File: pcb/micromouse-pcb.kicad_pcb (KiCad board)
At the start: 4 copper layers, 100 x 114 mm, 154 parts, among them J1 JST_PH_B2B-PH-K_1x02_P2.00mm_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, J10 PinSocket_1x08_P2.54mm_Vertic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, J11 PinSocket_1x08_P2.54mm_Vertic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, J2 PinHeader_1x02_P2.54mm_Vertic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, J5 JST_PH_B6B-PH-K_1x06_P2.00mm_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, J6 JST_PH_B6B-PH-K_1x06_P2.00mm_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, J7 USB_C_Receptacle_GCT_USB4105-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, J8 PinHeader_1x06_P2.54mm_Vertic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, Q1 SOT-23, Q10 LED_1206_3216Metric, Q11 LED_1206_3216Metric, Q12 LED_1206_3216Metric, Q13 LED_1206_3216Metric, Q14 LED_1206_3216Metric, Q15 LED_1206_3216Metric, Q16 SOT-23, Q17 SOT-23, Q18 SOT-23, Q19 SOT-23, Q2 LED_D3.0mm_Clear, Q20 SOT-23, Q21 SOT-23, Q22 SOT-23, Q23 SOT-23, Q24 SOT-23, Q25 SOT-23, Q26 SOT-23, Q27 SOT-23, Q28 SOT-23, Q29 SOT-23, Q3 LED_D3.0mm_Clear, Q30 SOT-23, Q31 SOT-23, Q32 SOT-23, Q33 SOT-23, Q4 LED_D3.0mm_Clear, Q5 LED_D3.0mm_Clear, Q6 LED_D3.0mm_Clear, Q7 LED_D3.0mm_Clear, Q8 LED_1206_3216Metric, Q9 LED_1206_3216Metric, SW1 SW_PUSH_6mm, SW2 SW_PUSH_6mm, SW3 SW_PUSH_6mm, SW4 SW_PUSH_6mm, U1 Texas_DRC0010J_ThermalVias, U3 ESP32-S3-WROOM-1, U4 SOIC-24W_7.5x15.4mm_P1.27mm, U6 SOT-23-6

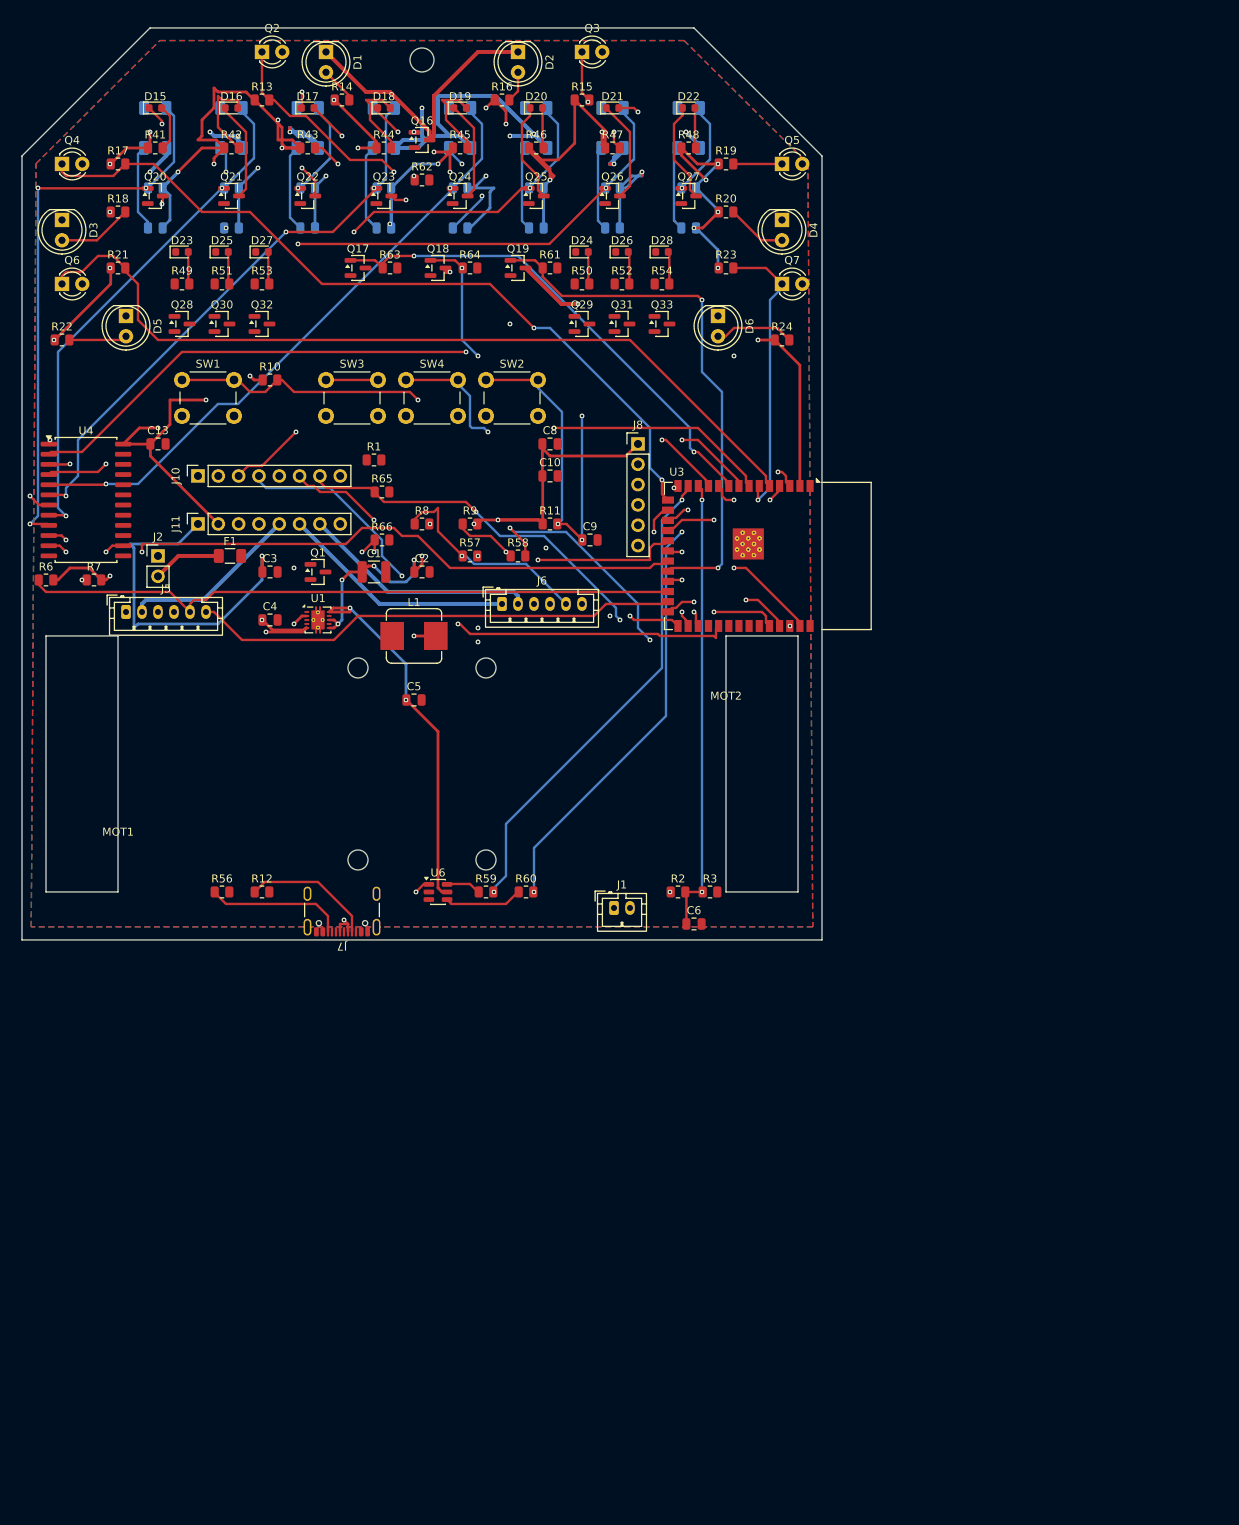
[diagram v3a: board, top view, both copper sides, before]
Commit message: Rev 5: SMD driver, rear service panel, bracket holes, routed to zero
- TB6612FNG as bare SSOP-24 in the inter-motor corridor; decoupling on B.Cu
- ESP32-S3-WROOM-1 moved to the rear, antenna overhanging the rear edge
  (Espressif-preferred); USB-C, ESD, JTAG and buttons A/B/C (+RST, silk
  letters) grouped around it as a service panel; motors moved forward
- Ø3.2mm/18.0mm-c-c NPTH pairs matching the printable UKMARSBot
  Pololu-pattern N20 bracket (STL link in README/PROJECT_NOTES)
- Wall sensors re-laid per parsed championship practice: detector forward,
  emitter 7.6mm behind, in-line, co-aimed; 10/45/75 degree aims
- USB VBUS turned into a cable-detect divider on IO37 (was a dangling NC)
- Board 100x120mm: +6mm rear fan-out band after routing proved density-bound
- board_geom.py: single source of mechanical truth (placement + router)
- Route-to-zero: jailed-first ordering with immediate retry ladders,
  hand bridges (D+ pair, VBUS stack link on In1), under-body pre-stitch,
  wide verify-proof retry rung, THT-aware clearance floors everywhere,
  all-layer via-replacement stitching, and heal_all.py convergent DRC healer
- Final: 0 unrouted, ERC 0, DRC 0 violations / 0 unconnected / 0 parity

Co-Authored-By: Claude Fable 5 <noreply@anthropic.com>
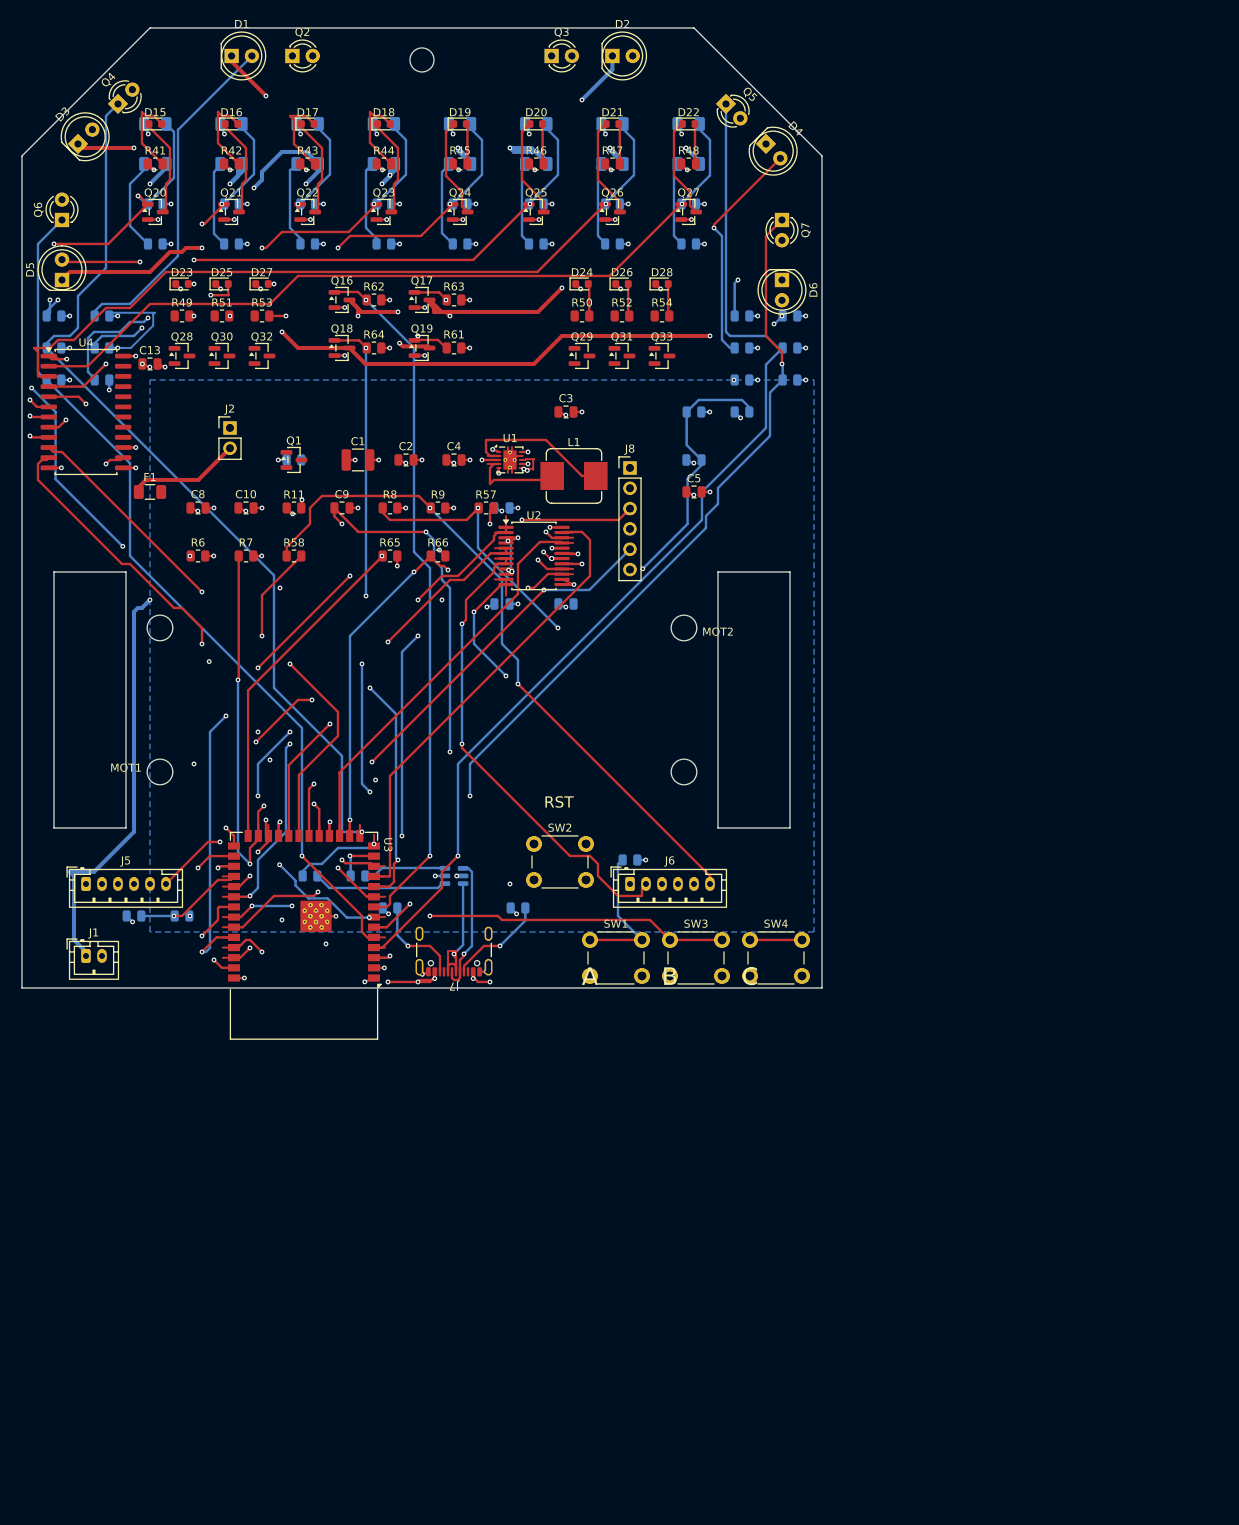
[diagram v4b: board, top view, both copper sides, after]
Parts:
- removed J10, J11: PinSocket_1x08_P2.54mm_Vertical, PinSocket_1x08_P2.54mm_Vertical
- added C11: 10uF, C_0805_2012Metric, B.Cu at (60.0, 72.0)
- added C12: 100nF, C_0805_2012Metric, B.Cu at (68.0, 72.0)
- added C14: 100nF, C_0805_2012Metric, B.Cu at (60.0, 60.0)
- added R67: R_0805_2012Metric, R_0805_2012Metric, B.Cu at (20.0, 111.0)
- added R68: R_0805_2012Metric, R_0805_2012Metric, B.Cu at (14.0, 111.0)
- added U2: SSOP-24_5.3x8.2mm_P0.65mm, SSOP-24_5.3x8.2mm_P0.65mm, F.Cu at (64.0, 66.0)
- C6, R1, R10, R12, R13, R14, R15, R16, R17, R18, R19, R2, R20, R21, R22, R23, R24, R3, R56, R59, R60, U6: moved to B.Cu
- moved SW1 86.6 mm to (71.0, 114.0)
- moved SW3 82.2 mm to (81.0, 114.0)
- moved SW4 82.2 mm to (91.0, 114.0)
- moved R10 75.0 mm to (76.0, 104.0), turned to 180 degrees
- moved U3 75.0 mm to (35.2, 113.5), turned to 180 degrees
- moved J1 66.3 mm to (8.00, 116.0)
- moved R3 60.1 mm to (90.0, 48.0), turned to 180 degrees
- moved R2 60.0 mm to (84.0, 48.0), turned to 180 degrees
- moved SW2 58.3 mm to (64.0, 102.0)
- moved C6 58.0 mm to (84.0, 54.0), turned to 180 degrees
- moved C8 44.7 mm to (22.0, 60.0)
- moved C5 43.6 mm to (84.0, 58.0)
- moved C3 42.1 mm to (68.0, 48.0)
- moved R14 40.4 mm to (10.0, 36.0), turned to 180 degrees
- moved R16 40.4 mm to (90.0, 36.0), turned to 180 degrees
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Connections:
- J7 pad A4: unconnected-(J7-VBUS-PadA4) -> USB_VBUS
- J7 pad A9: unconnected-(J7-VBUS-PadA4) -> USB_VBUS
- J7 pad B4: unconnected-(J7-VBUS-PadA4) -> USB_VBUS
- J7 pad B9: unconnected-(J7-VBUS-PadA4) -> USB_VBUS
- U3 pad 30: unconnected-(U3-IO37-Pad30) -> VBUS_SENSE
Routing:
- net PLUS3V3: track 602.5 -> 70.9 mm, vias 39 -> 54
- net VM_BATT: track 154.8 -> 19.6 mm, vias 9 -> 11
- net EMIT_DIAG_K: track 0.00 -> 111.3 mm, vias 0 -> 3
- net GND: track 0.00 -> 100.7 mm, vias 0 -> 69
- net JTAG_TDO: track 0.00 -> 93.1 mm, vias 0 -> 2
- net WALL4_SENSE: track 51.0 -> 134.5 mm
- net JTAG_TMS: track 0.00 -> 82.4 mm, vias 0 -> 1
- net JTAG_TCK: track 0.00 -> 79.2 mm, vias 0 -> 4
- net WALL2_SENSE: track 82.7 -> 161.6 mm, vias 2 -> 3
- net WALL6_SENSE: track 37.0 -> 113.6 mm, vias 1 -> 3
- net JTAG_TDI: track 0.00 -> 74.6 mm, vias 0 -> 4
- net ENC2_B: track 22.9 -> 85.1 mm, vias 1 -> 2
- net USB_VBUS: track 0.00 -> 56.6 mm, vias 0 -> 6
- net USB_DM: track 60.9 -> 5.54 mm, vias 2 -> 1
- net EMIT_FRONT_K: track 36.6 -> 91.3 mm, vias 0 -> 4
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- added copper zone on In1.Cu, net GND
- added copper zone on In2.Cu, net PLUS3V3
- added copper zone on B.Cu, net VM_BATT
- removed copper zone on B.Cu, net GND
- removed copper zone on F.Cu, net GND
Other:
- board size 100 x 114 mm -> 100 x 120 mm
- board text added: "A"
- board text added: "B"
- board text added: "C"
- board text added: "RST"

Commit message: Rev 5.1: fix floating FETs (audit-caught), NPTH bracket holes, hard gates
An adversarial audit of shipped rev 5 found Q1 + Q28-Q33 electrically
floating: Device:Q_PMOS numbers its pins D/G/S, the SOT-23 pads are 1/2/3,
and PcbGen silently skipped unmatched pads -- netless pads make no ratsnest,
so both the router and DRC connectivity were structurally blind. The battery
power path (J2 -> F1 -> Q1 -> VM_BATT) was open and all six wall-indicator
drivers were dead. Full postmortem in PROJECT_NOTES.md.

- QPMOS now instantiates Transistor_FET:Q_PMOS_GSD (pins 1/2/3, same
  geometry); netlist verified pin-by-pin, board rerouted to zero
- NEW hard gate: PcbGen.assert_netlist_pads_mapped() in build_pcb.py --
  every netlist (ref,pin) must exist as a board pad carrying that net
- net_conflict parity severity raised warning -> error in .kicad_pro
- verify_netlist.py rewritten for rev-5 topology (was rev-1 names, always
  exit 0); now checks the battery path and sensor->reader->indicator
  reachability, exits 1 on failure
- Mounting holes converted from Edge.Cuts circles to real NPTH pads
  (H1-H5, board-only footprints): drilled, in the fab hole table, matching
  the documented "Ø3.2mm NPTH" claim; keepouts now admit footprint pads
- heal_all.py: no more stacked bridge vias on unfixable fragments
- Docs: U3 anchor corrected to (35.25,113.5); stale rev-3/4 renders removed
- Verified: ERC 0 | DRC 0 violations / 0 unconnected / 0 parity (with
  net_conflict at error severity) | verify_netlist PASSES | 454/454 pins
  mapped | Q1 pads on Net-(Q1-G)/VM_BATT/Net-(Q1-D) with routed copper

Co-Authored-By: Claude Fable 5 <noreply@anthropic.com>
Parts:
- added H1: , MountingHole_NPTH, F.Cu at (17.2, 75.0)
- added H2: , MountingHole_NPTH, F.Cu at (17.2, 93.0)
- added H3: , MountingHole_NPTH, F.Cu at (82.8, 75.0)
- added H4: , MountingHole_NPTH, F.Cu at (82.8, 93.0)
- added H5: , MountingHole_NPTH, F.Cu at (50.0, 4.00)
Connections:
- F1 pad 2: Net-(F1-Pad2) -> Net-(Q1-D)
- Q1 pad 1: (no net) -> Net-(Q1-G)
- Q1 pad 2: (no net) -> VM_BATT
- Q1 pad 3: (no net) -> Net-(Q1-D)
- Q28 pad 1: (no net) -> WALL1_SENSE
- Q28 pad 2: (no net) -> PLUS3V3
- Q28 pad 3: (no net) -> Net-(Q28-D)
- Q29 pad 1: (no net) -> WALL2_SENSE
- Q29 pad 2: (no net) -> PLUS3V3
- Q29 pad 3: (no net) -> Net-(Q29-D)
- Q30 pad 1: (no net) -> WALL3_SENSE
- Q30 pad 2: (no net) -> PLUS3V3
- Q30 pad 3: (no net) -> Net-(Q30-D)
- Q31 pad 1: (no net) -> WALL4_SENSE
- Q31 pad 2: (no net) -> PLUS3V3
- Q31 pad 3: (no net) -> Net-(Q31-D)
- Q32 pad 1: (no net) -> WALL5_SENSE
- Q32 pad 2: (no net) -> PLUS3V3
- Q32 pad 3: (no net) -> Net-(Q32-D)
- Q33 pad 1: (no net) -> WALL6_SENSE
- Q33 pad 2: (no net) -> PLUS3V3
- Q33 pad 3: (no net) -> Net-(Q33-D)
- R1 pad 1: Net-(Q1-PadG) -> Net-(Q1-G)
- R49 pad 1: Net-(Q28-PadD) -> Net-(Q28-D)
- R50 pad 1: Net-(Q29-PadD) -> Net-(Q29-D)
- R51 pad 1: Net-(Q30-PadD) -> Net-(Q30-D)
- R52 pad 1: Net-(Q31-PadD) -> Net-(Q31-D)
- R53 pad 1: Net-(Q32-PadD) -> Net-(Q32-D)
- R54 pad 1: Net-(Q33-PadD) -> Net-(Q33-D)
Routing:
- net JTAG_TDI: track 74.6 -> 106.5 mm
- net USER_BTN2: track 78.1 -> 109.0 mm, vias 3 -> 4
- net Net-(Q28-D): track 0.00 -> 30.4 mm
- net Net-(D5-A): track 31.4 -> 54.6 mm, vias 2 -> 3
- net Net-(D3-A): track 34.7 -> 57.4 mm, vias 1 -> 2
- net WALL5_SENSE: track 110.3 -> 132.1 mm, vias 1 -> 3
- net Net-(Q1-D): track 0.00 -> 21.5 mm
- net USER_BTN: track 101.5 -> 121.6 mm, vias 6 -> 7
- net WALL6_SENSE: track 113.6 -> 131.8 mm
- net WALL2_SENSE: track 161.6 -> 178.2 mm, vias 3 -> 4
- net EMIT_FRONT_K: track 91.3 -> 106.2 mm, vias 4 -> 2
- net WALL4_SENSE: track 134.5 -> 148.5 mm, vias 1 -> 3
- net Net-(Q30-D): track 0.00 -> 13.7 mm, vias 0 -> 3
- net MUX_S1: track 65.6 -> 78.5 mm
- net WALL3_SENSE: track 115.7 -> 127.7 mm, vias 1 -> 5
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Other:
- outline, holes or cut-outs redrawn

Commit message: Rev 5.2: verified-MPN BOM, complete STEP coverage, gated fab exports
Closes the three deferred audit items:

- BOM.csv: 42 line items, 100% MPN coverage. Every part adversarially
  verified against datasheets + live distributor stock (31 parts, two
  research passes): packages vs footprints, SOT-23 FET pinouts (1=G/2=S/3=D).
  Catches: USBLC6-2P6 would have been the wrong package (SOT-666) -> 2SC6;
  module pinned to -N16 (octal-PSRAM variants consume IO35-37 which this
  design uses); L1 -> SRP7028A-1R5M (datasheet-typical 1.5uH, verified
  orderable); line array = IR11-21C/TR8 + PT11-21B/L41/TR8 (true 1206,
  daylight-filtered PT required). SOURCING ALARM: SFH 309 FA is Last Time
  Buy 2026-12-01.
- MPN/Manufacturer emitted as hidden schematic fields via a gen_sch
  field_provider; fixed latent value-plumbing bug (photo_val/led_val never
  passed -- SMD line parts were VALUE-labeled as THT parts); 147 board
  Value fields re-synced; net topology proven byte-identical.
- gen_step_models.py: hand-authored AP214 box-solid STEP for the N20 motors
  and for U1/L1 (KiCad ships no models for those footprints); U1/L1
  repointed to project-local models (text-level -- pcbnew Models() is a
  SWIG copy); STEP export now loads EVERY model.
- export_fab.py: gerbers/drill/pos/STEP/BOM with hard gates (3.2+3.0mm NPTH
  tools must be in the drill data, no missing 3D models, all layers
  non-trivial, BOM MPN coverage reported). ALL GATES PASSED.
- Final state unchanged and re-verified: ERC 0, DRC 0/0/0, netlist gate
  passes.

Co-Authored-By: Claude Fable 5 <noreply@anthropic.com>
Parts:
- C10: value C_0805_2012Metric -> 10uF
- C13, C6, C8: value C_0805_2012Metric -> 100nF
- C9: value C_0805_2012Metric -> 1uF
- D1, D2, D3, D4, D5, D6: value LED_D5.0mm_IRGrey -> SFH4550 (THT, LD271 base symbol)
- D10, D11, D12, D13, D14, D7, D8, D9: value LED_1206_3216Metric -> IR11-21C 940nm 1206 IR emitter (LD271 sym for ERC)
- D15, D16, D17, D18, D19, D20, D21, D22: value LED_0603_1608Metric -> Indicator LED 0603 super-red AlInGaP, high-efficiency bin REQUIRED at 1.4mA (e.g. Kingbright APT1608SURCK; LD271 base s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
- D23, D24, D25, D26, D27, D28: value LED_0603_1608Metric -> Indicator LED 0603 super-red AlInGaP, high-eff bin (e.g. APT1608SURCK)
- F1: value Fuse_1206_3216Metric -> 2A_resettable
- J1: value JST_PH_B2B-PH-K_1x02_P2.00mm_Vertical -> BATT_IN_1S
- J2: value PinHeader_1x02_P2.54mm_Vertical -> EXT_SWITCH
- J5: value JST_PH_B6B-PH-K_1x06_P2.00mm_Vertical -> MOTOR_A_N20_ENCODER
- J6: value JST_PH_B6B-PH-K_1x06_P2.00mm_Vertical -> MOTOR_B_N20_ENCODER
- J7: value USB_C_Receptacle_GCT_USB4105-xx-A_16P_TopMnt_Horizontal -> USB-C rear (GCT USB4105; VBUS unused -- battery powers the board)
- J8: value PinHeader_1x06_P2.54mm_Vertical -> JTAG_1x6 (3V3,TMS,TCK,TDO,TDI,GND)
- Q1: value SOT-23 -> Q_PMOS low-Vth (e.g. DMP2035U-7)
- Q10, Q11, Q12, Q13, Q14, Q15, Q8, Q9: value LED_1206_3216Metric -> PT11-21B/L41 940nm 1206 phototransistor, DAYLIGHT-FILTERED (black lens) REQUIRED -- an unfiltered part (PT11-21C) re-op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
- Q16, Q17, Q18, Q19, Q20, Q21, Q22, Q23, Q24, Q25, Q26, Q27: value SOT-23 -> BSS138 (real part; Q_NMOS_GSD base symbol used so ERC checks pins)
- Q2, Q3, Q4, Q5, Q6, Q7: value LED_D3.0mm_Clear -> SFH309
- Q28, Q29, Q30, Q31, Q32, Q33: value SOT-23 -> BSS84 (PMOS indicator driver; Q_PMOS base symbol)
- R1, R61, R62, R63, R64: value R_0805_2012Metric -> 100k
- R10, R11, R6, R65, R66, R67, R7, R8, R9: value R_0805_2012Metric -> 10k
- R12, R56: value R_0805_2012Metric -> 5.1k
- R13, R15, R17, R19, R21, R23, R25, R27, R29, R31, R33, R35, R37, R39: value R_0805_2012Metric -> 47k
- R14, R16, R18, R20, R22, R24: value R_0805_2012Metric -> 33
- R2: value R_0805_2012Metric -> 22k
- R26, R28, R30, R32, R34, R36, R38, R40: value R_0805_2012Metric -> 120
- R3: value R_0805_2012Metric -> 33k
- R41, R42, R43, R44, R45, R46, R47, R48, R49, R50, R51, R52, R53, R54, R57, R58: value R_0805_2012Metric -> 1k
- R59, R60: value R_0805_2012Metric -> 22
- R68: value R_0805_2012Metric -> 15k
- SW1: value SW_PUSH_6mm -> BTN_A (start / BOOT)
- SW2: value SW_PUSH_6mm -> RESET
- SW3: value SW_PUSH_6mm -> BTN_B
- SW4: value SW_PUSH_6mm -> BTN_C
- U1: value Texas_DRC0010J_ThermalVias -> TPS63001 (fixed 3.3V buck-boost; TPS63000 base symbol so ERC checks pins)
- U2: value SSOP-24_5.3x8.2mm_P0.65mm -> TB6612FNG
- U3: value ESP32-S3-WROOM-1 -> ESP32-S3-WROOM-1-N16 (non-R8: octal-PSRAM variants lose IO35-37 = buttons 2/3)
- U4: value SOIC-24W_7.5x15.4mm_P1.27mm -> CD74HC4067M
- U6: value SOT-23-6 -> USBLC6-2SC6 (SOT-23-6; 2P6 base symbol so ERC checks pins)
